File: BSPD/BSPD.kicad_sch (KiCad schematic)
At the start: 58 parts, among them J2 Conn_01x04, J3 Conn_01x02, K2 G2RL-2, Q1 AO3401A, Q2 BSS138, Q3 BSS138, U2 AMS1117-5.0

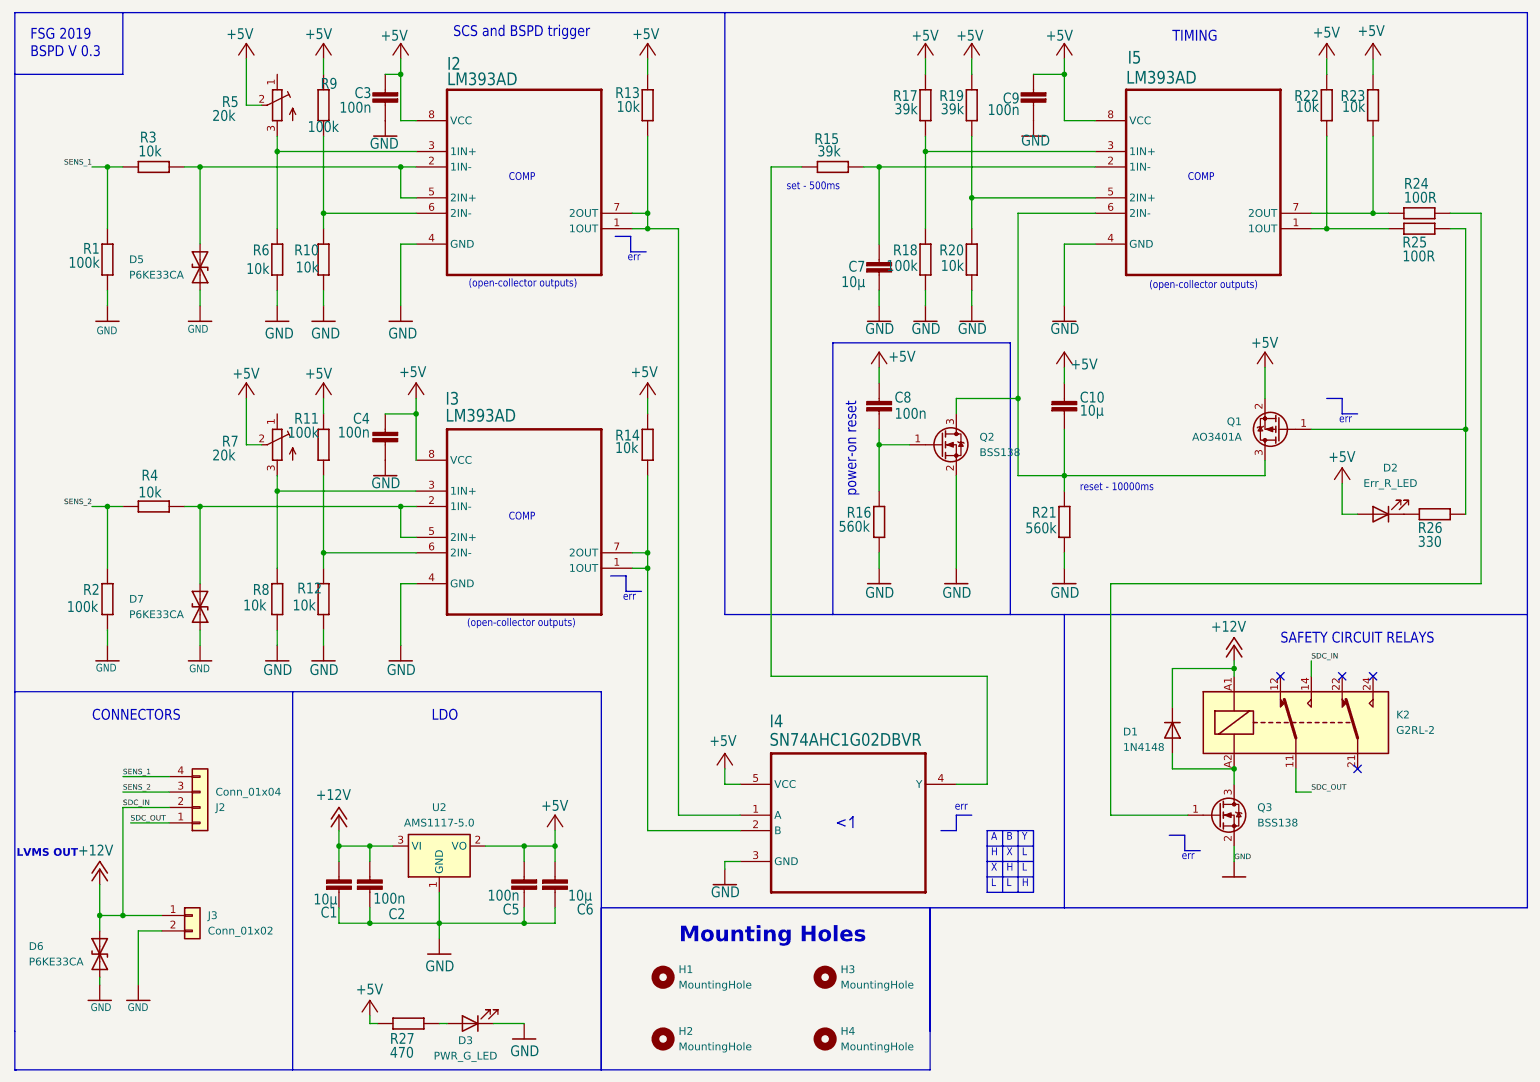
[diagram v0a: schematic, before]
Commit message: Increase width of SDC track
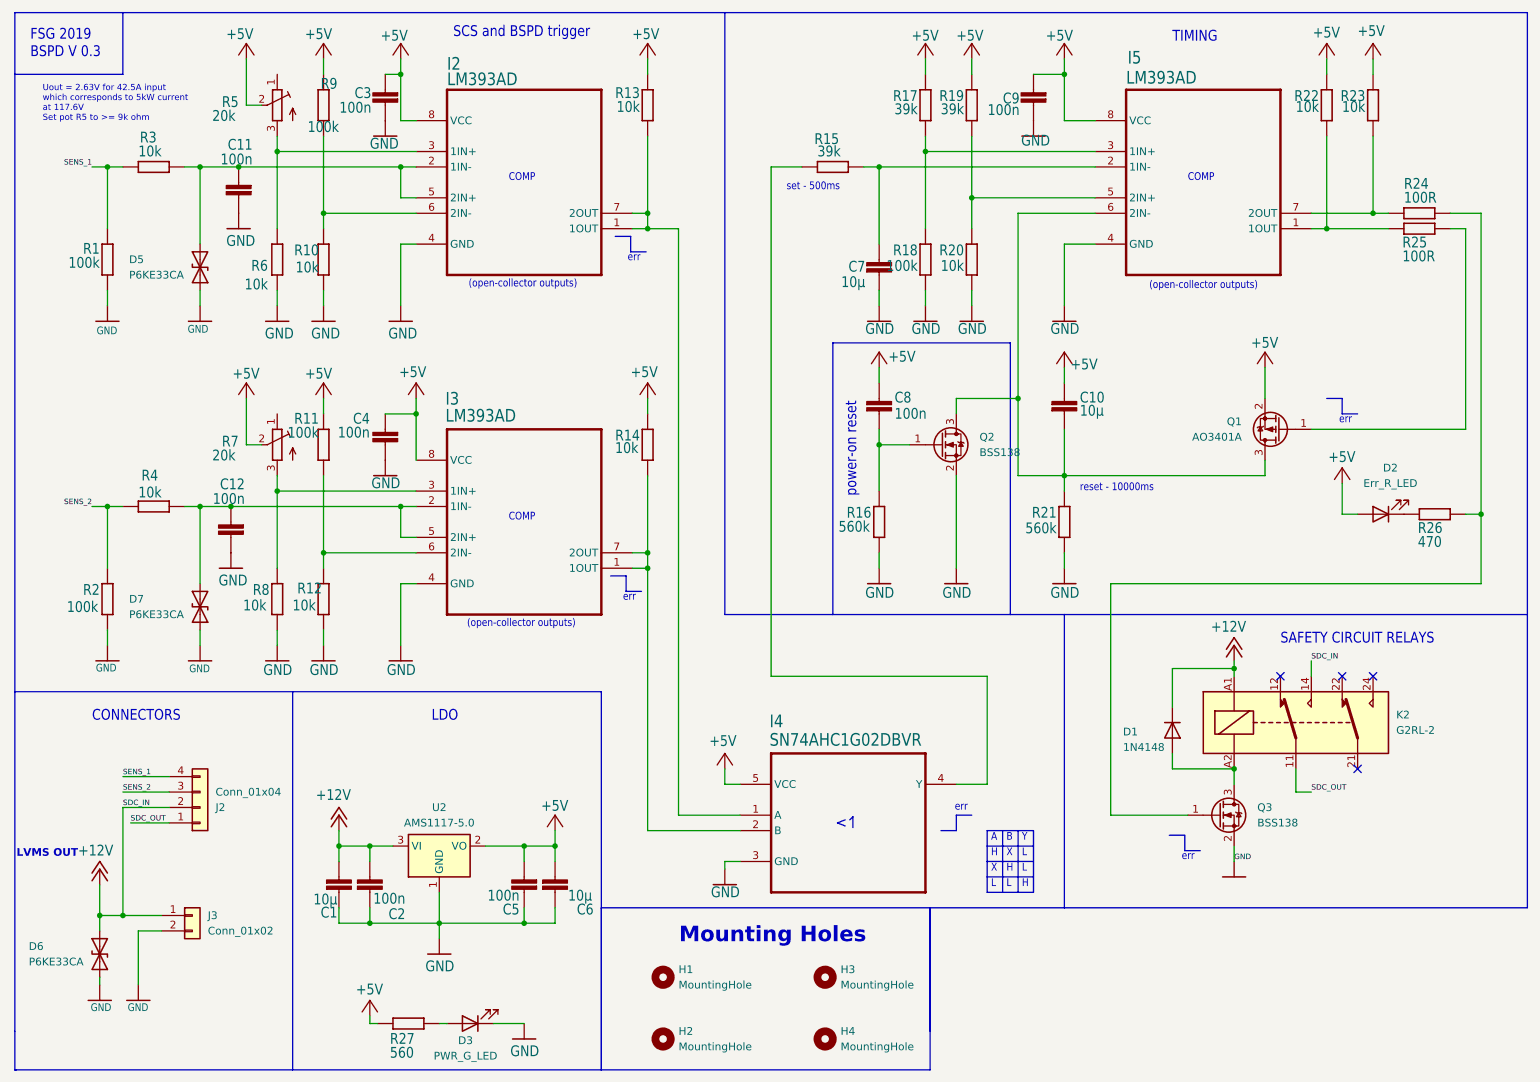
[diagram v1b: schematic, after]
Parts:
- added C11, C12: 100n, Capacitor_SMD:C_0603_1608Metric_Pad1.08x0.95mm_HandSolder, symbol FSG_2019_BSPD_0.3-eagle-import:resistor_C-EUC0603
- R26: value 330 -> 470
- R27: value 470 -> 560
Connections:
- net GND: now also C11.1, C12.1
- net at D7.2 (A2), I3.2 (1IN-), I3.5 (2IN+)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: now also C12.2
- net at D5.2 (A2), I2.2 (1IN-), I2.5 (2IN+)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: now also C11.2
- net at Q1.1 (G), R25.1: no longer R26.1
- net at Q3.1 (G), R24.1: now also R26.1
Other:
- note added: "Uout = 2.63V for 42.5A input which corresponds to 5kW current at 117.6V Set pot R5 to >= 9k ohm"

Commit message: Precharge modifications
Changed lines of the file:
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@@
 		(on_board yes)
 		(dnp no)
-		(fields_autoplaced yes)
 		(property "Reference" "Q2"
-			(at 180.34 85.0899 0)
+			(at 179.578 85.344 0)
 			(effects
 				(font
@@
 		)
 		(property "Value" "BSS138"
-			(at 180.34 87.6299 0)
+			(at 179.578 87.884 0)
 			(effects
 				(font

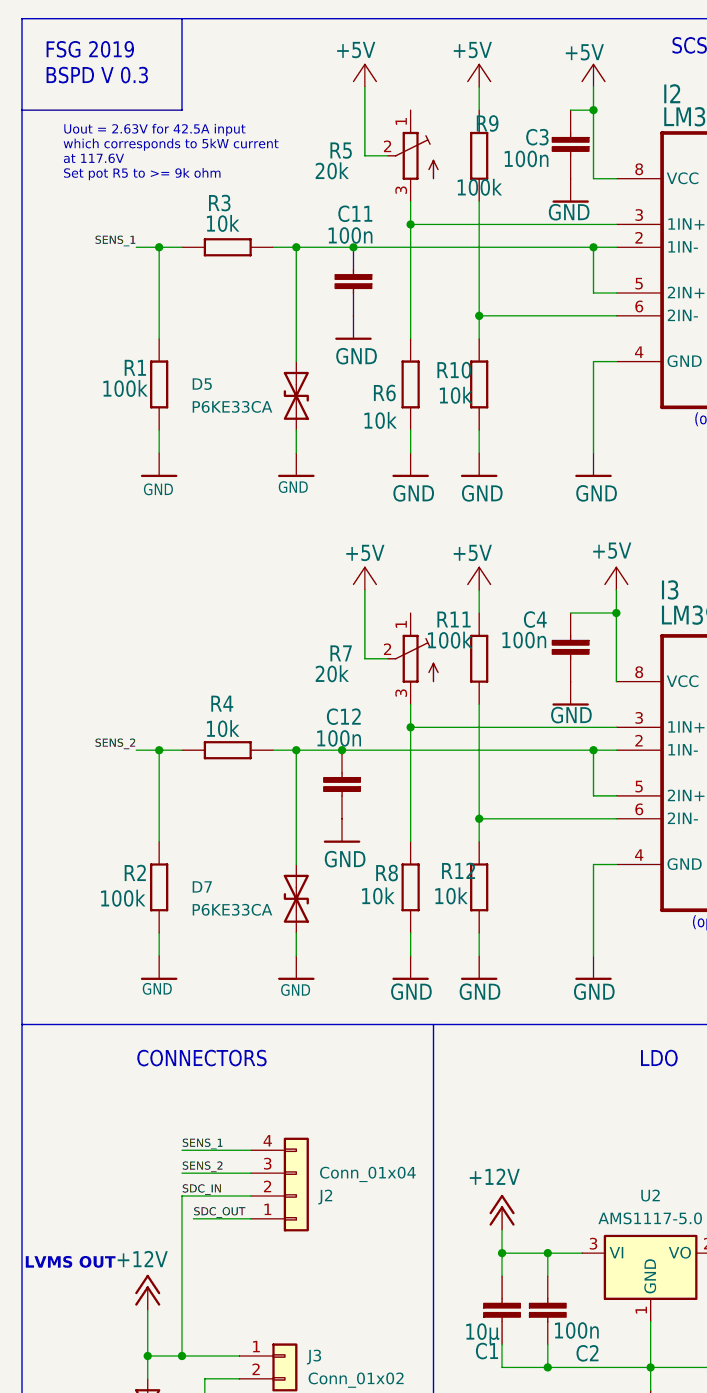
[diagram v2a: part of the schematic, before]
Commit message: added hierarchichal labels for hierarchical sheet compatibility
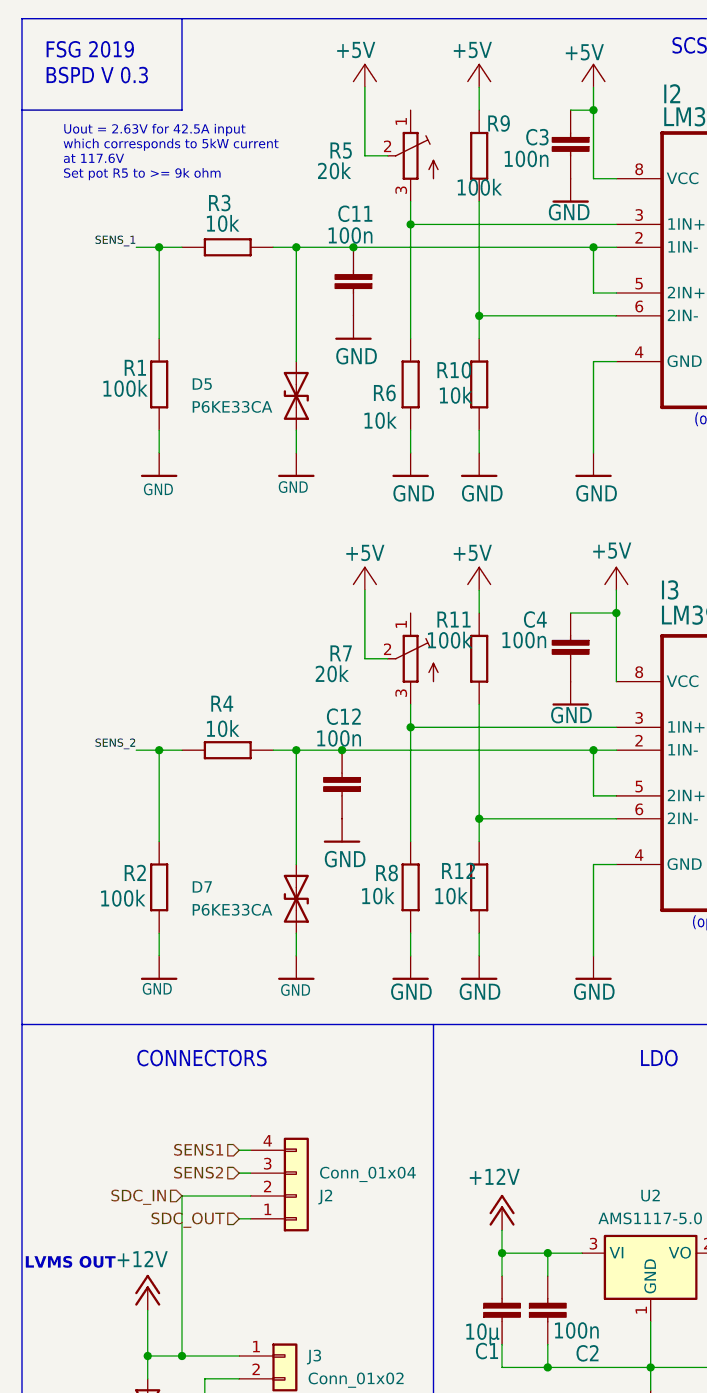
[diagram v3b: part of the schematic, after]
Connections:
- net SENS_1: no longer J2.4 (Pin_4)
- net SENS_2: no longer J2.3 (Pin_3)
- new net SENS1: J2.4 (Pin_4)
- new net SENS2: J2.3 (Pin_3)

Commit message: Save corrupted files and new modifications
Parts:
- K2: value G2RL-2 -> G2RL-1-E
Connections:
- net SENS1 is gone; now on net SENS_1: J2.4 (Pin_4)
- net SENS2 is gone; now on net SENS_2: J2.3 (Pin_3)
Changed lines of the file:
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@@
 		)
 	)
-	(hierarchical_label "SENS1"
+	(hierarchical_label "SENS_1"
 		(shape input)
 		(at 45.72 140.97 180)
@@
 		)
 	)
-	(hierarchical_label "SENS2"
+	(hierarchical_label "SENS_2"
 		(shape input)
 		(at 45.72 143.51 180)
@@
 			)
 		)
-		(property "Value" "G2RL-2"
+		(property "Value" "G2RL-1-E"
 			(at 248.92 133.3499 0)
 			(effects
